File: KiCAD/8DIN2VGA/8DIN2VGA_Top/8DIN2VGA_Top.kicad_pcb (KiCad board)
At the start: 2 copper layers, 7.2 x 20 mm, 2 parts, among them P1 DIN_TOP, P2 DIN_TOP_TO_MAIN

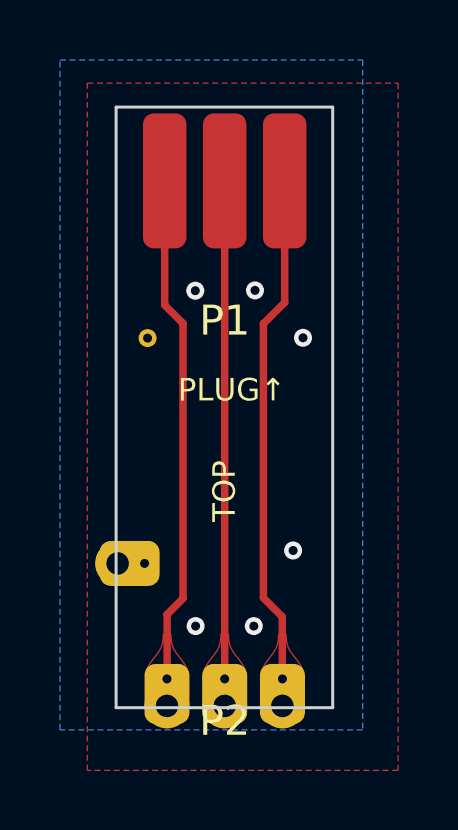
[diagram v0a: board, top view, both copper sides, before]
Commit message: Update with new 5V design
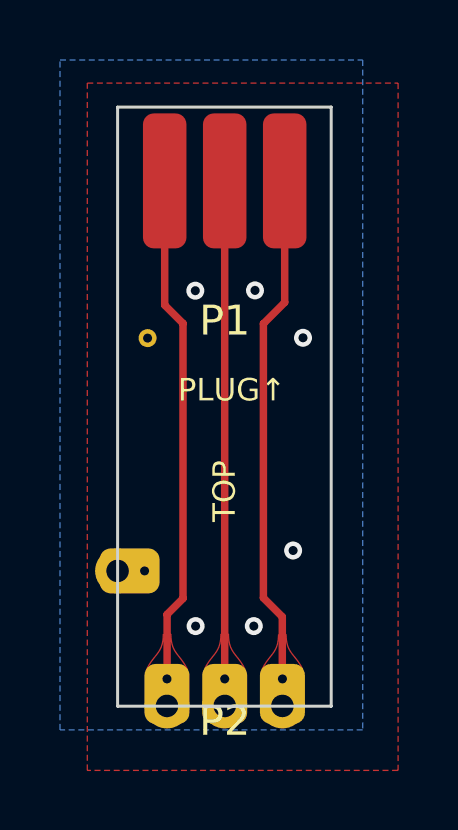
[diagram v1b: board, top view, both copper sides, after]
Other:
- board size 7.2 x 20 mm -> 7.1 x 20 mm
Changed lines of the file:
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@@
-(kicad_pcb (version 20171130) (host pcbnew "(5.1.8-0-10_14)")
+(kicad_pcb (version 20171130) (host pcbnew "(5.1.10-1-10_14)")
   (general
     (thickness 0.8)
@@
     (pad 8 thru_hole circle (at -1.924 0) (size 1.5 1.5) (drill 0.75) (layers *.Cu *.Mask)
       (net 2 /Red))
-    (pad 4 thru_hole roundrect (at -2.67 -4.75 270) (size 1.5 2) (drill 0.3 (offset 0 0.5)) (layers *.Cu *.Mask) (roundrect_rratio 0.25)
+    (pad 4 thru_hole roundrect (at -2.67 -4.5 270) (size 1.5 2) (drill 0.3 (offset 0 0.5)) (layers *.Cu *.Mask) (roundrect_rratio 0.25)
       (net 4 /GND))
-    (pad 4 thru_hole circle (at -3.57 -4.75 270) (size 1.5 1.5) (drill 0.75) (layers *.Cu *.Mask)
+    (pad 4 thru_hole circle (at -3.57 -4.5 270) (size 1.5 1.5) (drill 0.75) (layers *.Cu *.Mask)
       (net 4 /GND))
   )
@@
     (effects (font (size 0.75 0.75) (thickness 0.1875)))
   )
-  (gr_line (start 148.6 111.46) (end 148.6 91.44) (layer Edge.Cuts) (width 0.1))
-  (gr_line (start 141.38 111.46) (end 148.6 111.46) (layer Edge.Cuts) (width 0.1))
-  (gr_line (start 141.38 91.44) (end 141.38 111.46) (layer Edge.Cuts) (width 0.1))
-  (gr_line (start 141.38 91.44) (end 148.6 91.44) (layer Edge.Cuts) (width 0.1))
+  (gr_line (start 148.55 111.41) (end 148.55 91.44) (layer Edge.Cuts) (width 0.1))
+  (gr_line (start 141.43 111.41) (end 148.55 111.41) (layer Edge.Cuts) (width 0.1))
+  (gr_line (start 141.43 91.44) (end 141.43 111.41) (layer Edge.Cuts) (width 0.1))
+  (gr_line (start 141.43 91.44) (end 148.55 91.44) (layer Edge.Cuts) (width 0.1))
   (segment (start 145 93.9) (end 145 109.23) (width 0.25) (layer Front) (net 1) (status 10))
   (segment (start 145 109.23) (end 145 110.49) (width 0.25) (layer Front) (net 1) (status 20))
